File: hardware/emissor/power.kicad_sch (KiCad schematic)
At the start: 17 parts, among them J2 USB-C, J3 5V EXT, U4 USBLC6-2SC6, U5 AP2112K-3.3

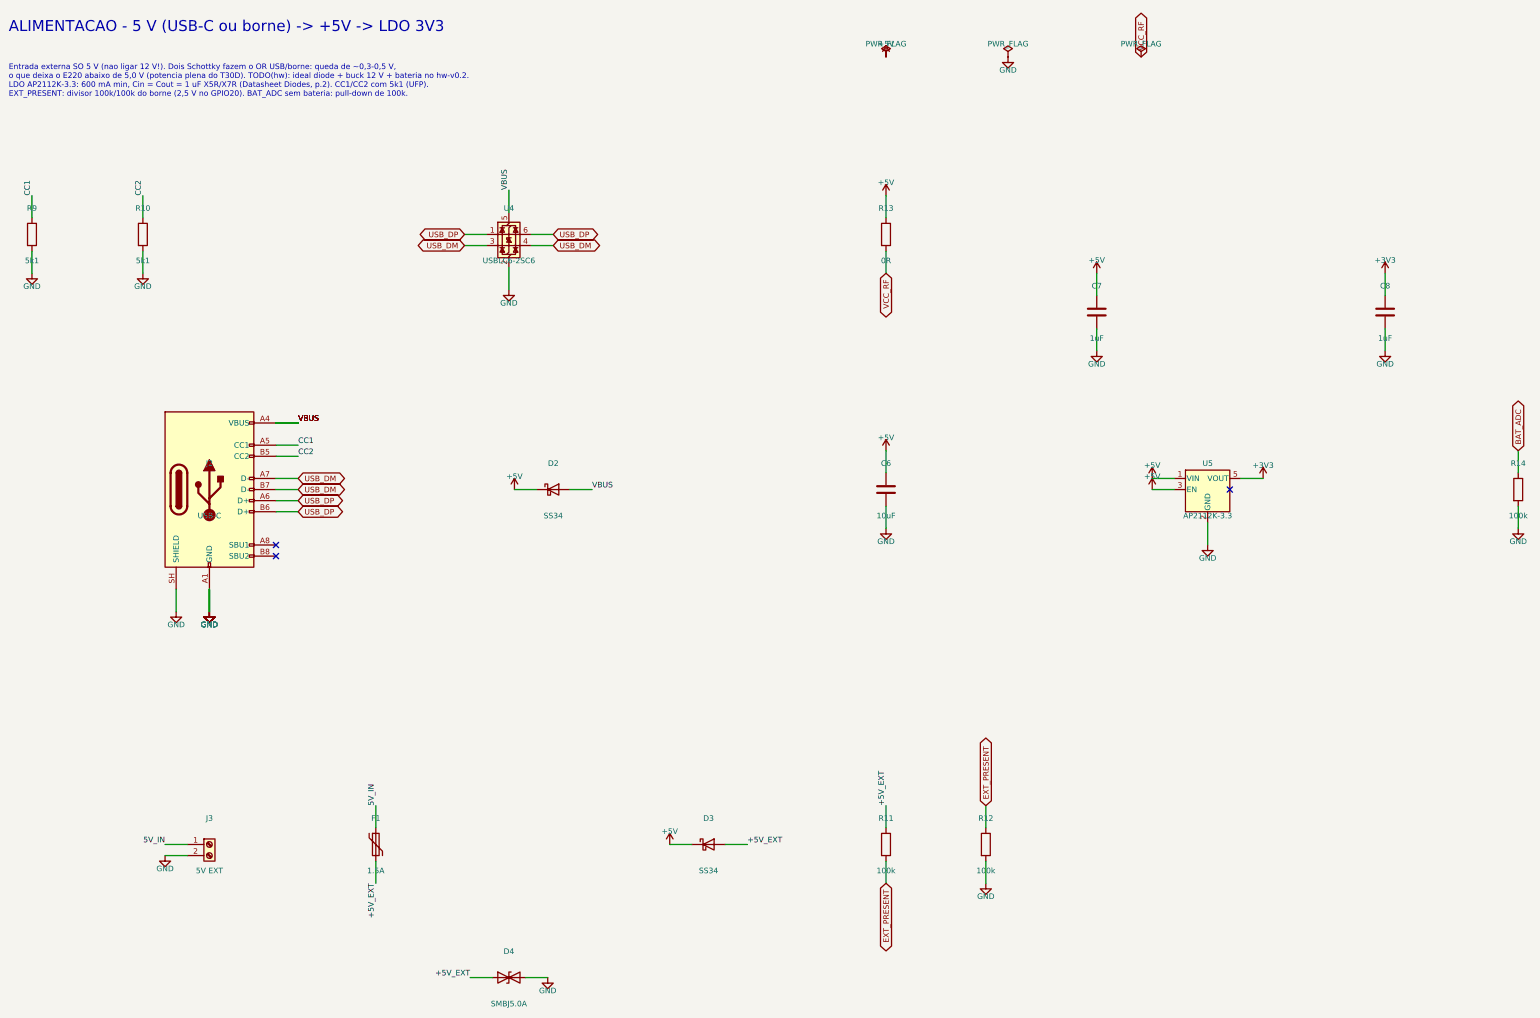
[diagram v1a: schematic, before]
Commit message: feat(hw): jack 12 V com buck AP63205, roteador proprio e serigrafia padronizada (receptor roteado; emissor com 1 net aberta)
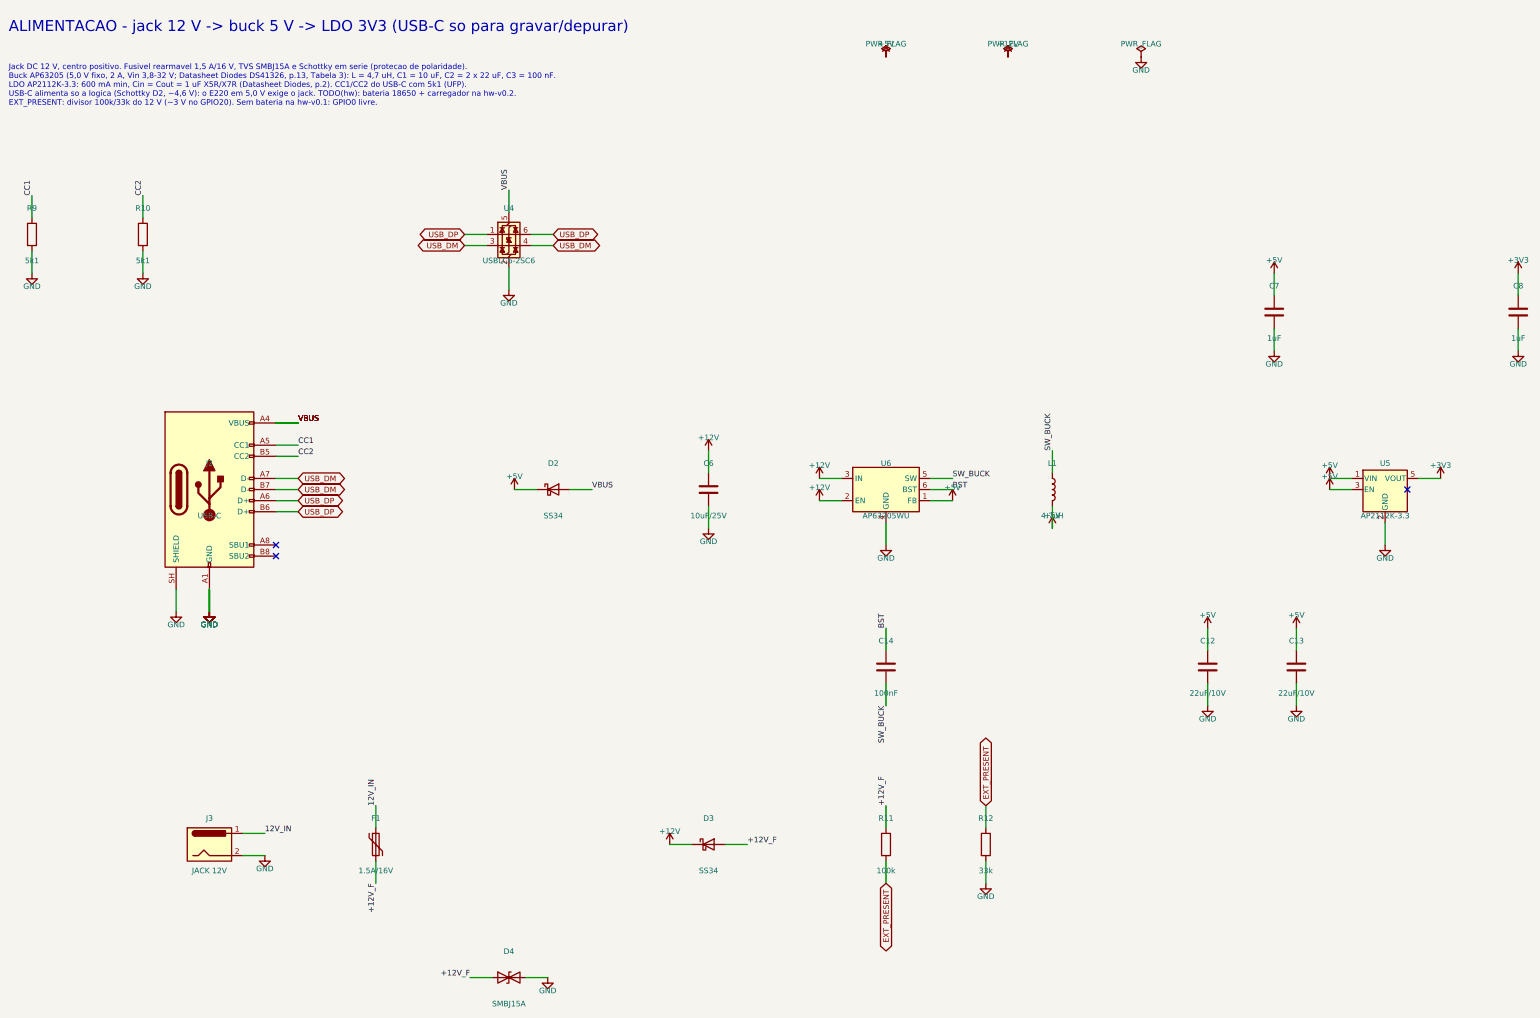
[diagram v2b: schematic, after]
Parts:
- removed J3: 5V EXT, TerminalBlock_Phoenix:TerminalBlock_Phoenix_MKDS-1,5-2-5.08_1x02_P5.08mm_Horizontal, symbol Connector:Screw_Terminal_01x02
- removed R13: 0R, Resistor_SMD:R_0603_1608Metric, symbol Device:R
- removed R14: 100k, Resistor_SMD:R_0603_1608Metric, symbol Device:R
- added C12, C13: 22uF/10V, Capacitor_SMD:C_0805_2012Metric, symbol Device:C
- added C14: 100nF, Capacitor_SMD:C_0603_1608Metric, symbol Device:C
- added J3: JACK 12V, lora-pump:BarrelJack_CUI_PJ-102AH_Horizontal, symbol Connector:Barrel_Jack
- added L1: 4.7uH, Inductor_SMD:L_Taiyo-Yuden_NR-60xx, symbol Device:L
- added U6: AP63205WU, Package_TO_SOT_SMD:TSOT-23-6, symbol Regulator_Switching:AP63205WU
- C6: value 10uF -> 10uF/25V; footprint Capacitor_SMD:C_0603_1608Metric -> Capacitor_SMD:C_0805_2012Metric; MPN CL10A106KP8NNNC -> CL21A106KAYNNNE
- D4: value SMBJ5.0A -> SMBJ15A; MPN SMBJ5.0A -> SMBJ15A
- F1: value 1.5A -> 1.5A/16V
- R12: value 100k -> 33k; MPN RC0603FR-07100KL -> RC0603FR-0733KL
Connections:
- net +5V: now also C12.1, C13.1, L1.2, U6.1 (FB); no longer C6.1, D3.1 (K)
- net GND: now also C12.2, C13.2, J3.2, U6.4 (GND)
- net +5V_EXT renamed +12V_F
- net 5V_IN renamed 12V_IN
- net 12V_IN: now also J3.1
- new net +12V: C6.1, D3.1 (K), U6.2 (EN), U6.3 (IN)
- new net BST: C14.1, U6.6 (BST)
- new net SW_BUCK: C14.2, L1.1, U6.5 (SW)
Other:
- note added: "ALIMENTACAO - jack 12 V -> buck 5 V -> LDO 3V3 (USB-C so para gravar/depurar)"
- note added: "Jack DC 12 V, centro positivo. Fusivel rearmavel 1,5 A/16 V, TVS SMBJ15A e Schottky em serie (protecao de polaridade). Buck AP63205 (5,0 V fixo, 2 A, Vin 3,8-32 V; Datasheet Diodes DS41326, p.13, Tabela 3): L = 4,7 uH, C1 = 10 uF, C2 = 2 x 22 uF, C3 = 100 nF. LDO AP2112K-3.3: 600 mA min, Cin = Cout = 1 uF X5R/X7R (Datasheet Diodes, p.2). CC1/CC2 do USB-C com 5k1 (UFP). USB-C alimenta so a logica 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"
- note removed: "ALIMENTACAO - 5 V (USB-C ou borne) -> +5V -> LDO 3V3"
- note removed: "Entrada externa SO 5 V (nao ligar 12 V!). Dois Schottky fazem o OR USB/borne: queda de ~0,3-0,5 V, o que deixa o E220 abaixo de 5,0 V (potencia plena do T30D). TODO(hw): ideal diode + buck 12 V + bateria no hw-v0.2. LDO AP2112K-3.3: 600 mA min, Cin = Cout = 1 uF X5R/X7R (Datasheet Diodes, p.2). CC1/CC2 com 5k1 (UFP). EXT_PRESENT: divisor 100k/100k do borne (2,5 V no GPIO20). BAT_ADC sem bateria: 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"
